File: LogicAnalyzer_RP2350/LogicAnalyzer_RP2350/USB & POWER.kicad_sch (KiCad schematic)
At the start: 14 parts, among them J2 2169890001, U1 TPS2552DRVR-1

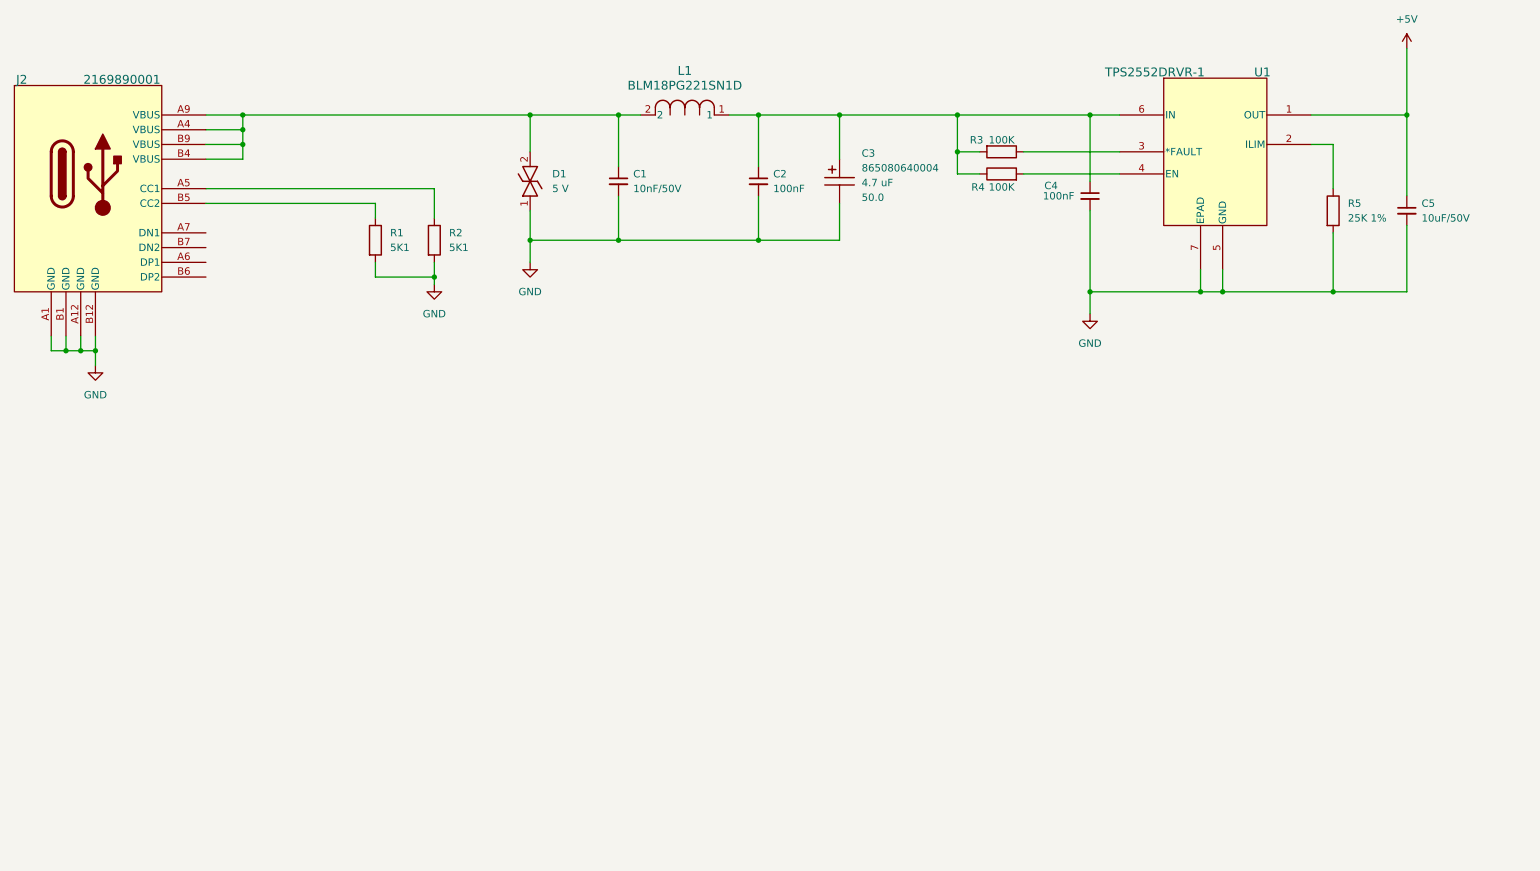
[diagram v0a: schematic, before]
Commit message: Added 3V3
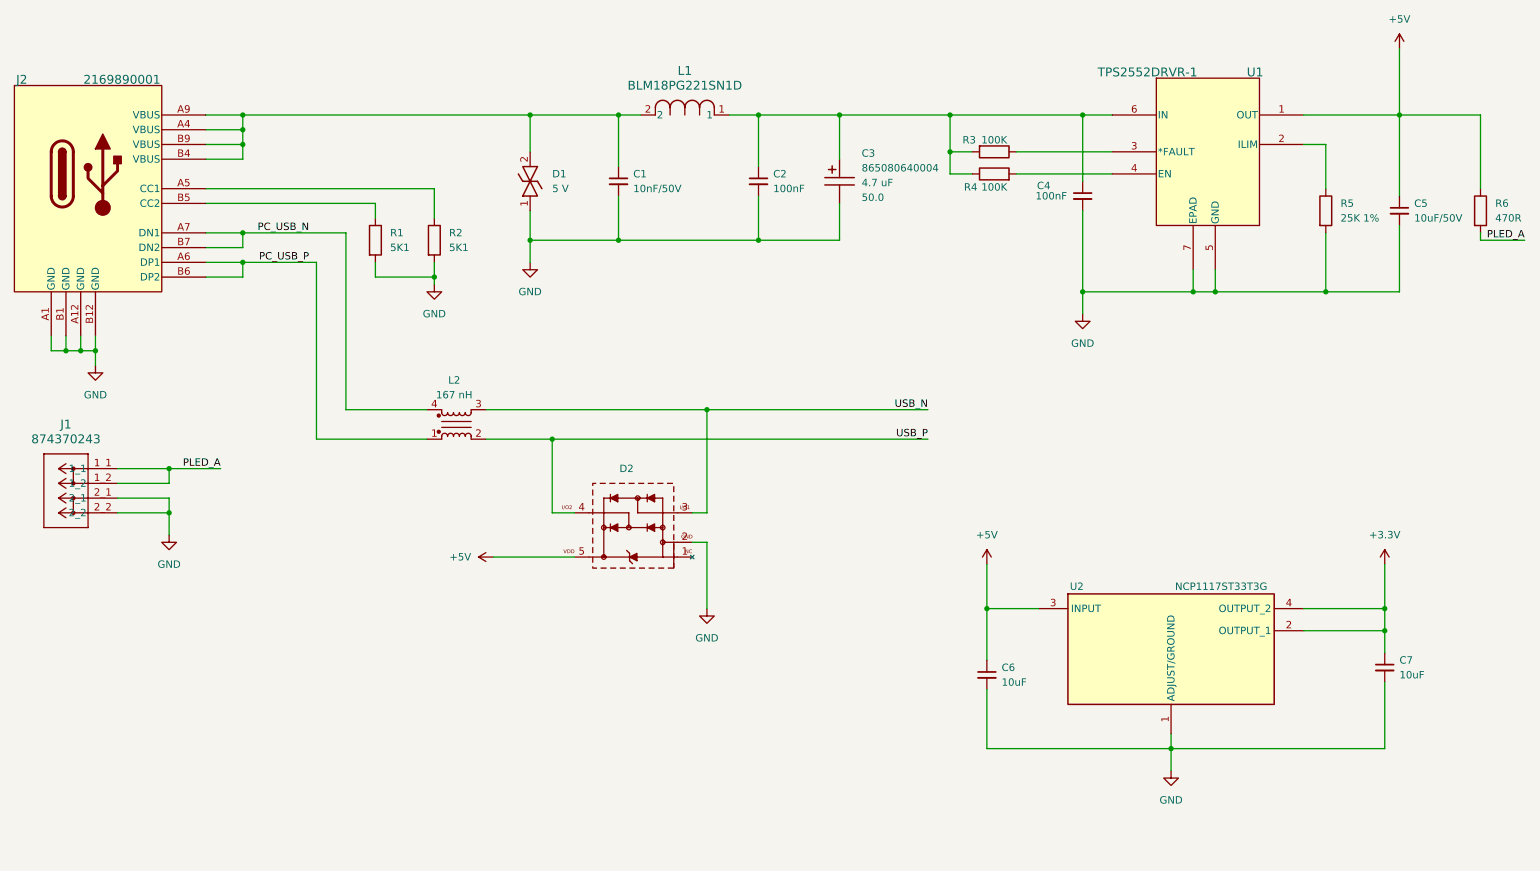
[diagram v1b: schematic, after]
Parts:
- added C6, C7: 10uF, Capacitor_SMD:C_0805_2012Metric_Pad1.18x1.45mm_HandSolder, symbol Device:C_Small
- added D2: SOT23-5L_824011, Diode_SMD_Wurth:D_Wurth_WE-TVS-SOT23-5L, symbol Diode_Wurth_WE-TVS:SOT23-5L_824011
- added J1: 874370243, CONN_874370231-SD_02_MOL, symbol Molex-0874370243:874370243
- added L2: 167 nH, Inductor_SMD_Wurth:L_Wurth_WE-CNSW-HF-0805, symbol Inductor_Wurth_WE-CNSW-HF:0805_744233121
- added R6: 470R, Resistor_SMD:R_0603_1608Metric_Pad0.98x0.95mm_HandSolder, symbol Device:R
- added U2: NCP1117ST33T3G, SOT230P700X180-4N, symbol NCP1117ST33T3G:NCP1117ST33T3G
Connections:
- net +5V: now also C6.1, D2.5 (VDD), R6.1, U2.3 (INPUT)
- net GND: now also C6.2, C7.2, D2.2 (GND), J1.2_1, J1.2_2, U2.1 (ADJUST/GROUND)
- net PC_USB_P: now reaches J2.A6 (DP1)
- net PC_USB_P: now also J2.B6 (DP2), L2.1
- net PC_USB_N: now reaches J2.A7 (DN1)
- net PC_USB_N: now also J2.B7 (DN2), L2.4
- new net +3.3V: C7.1, U2.2 (OUTPUT_1), U2.4 (OUTPUT_2)
- new net PLED_A: J1.1_1, J1.1_2, R6.2
- new net USB_N: D2.3 (I/O1), L2.3
- new net USB_P: D2.4 (I/O2), L2.2
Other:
- moved on the sheet: C4, C5, R3, R4, R5, U1

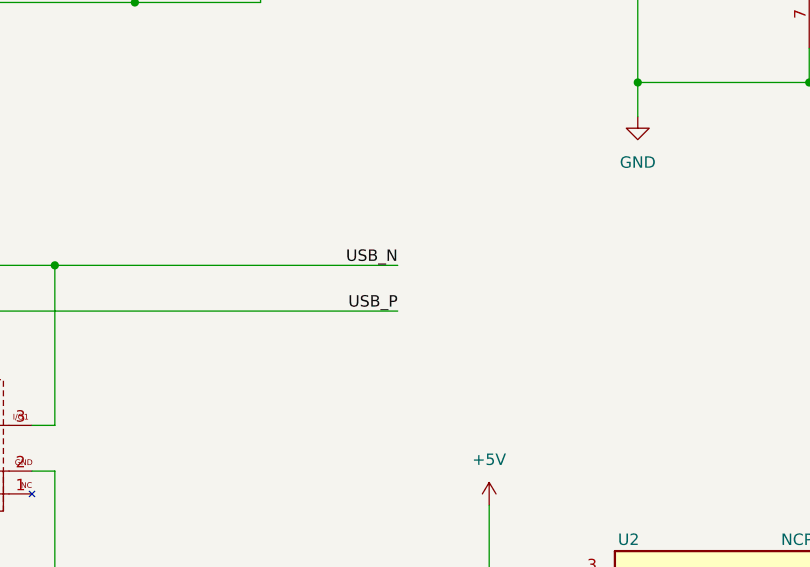
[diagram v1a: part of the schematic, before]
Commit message: added RP2350 Child Sheets and H Nets for USB
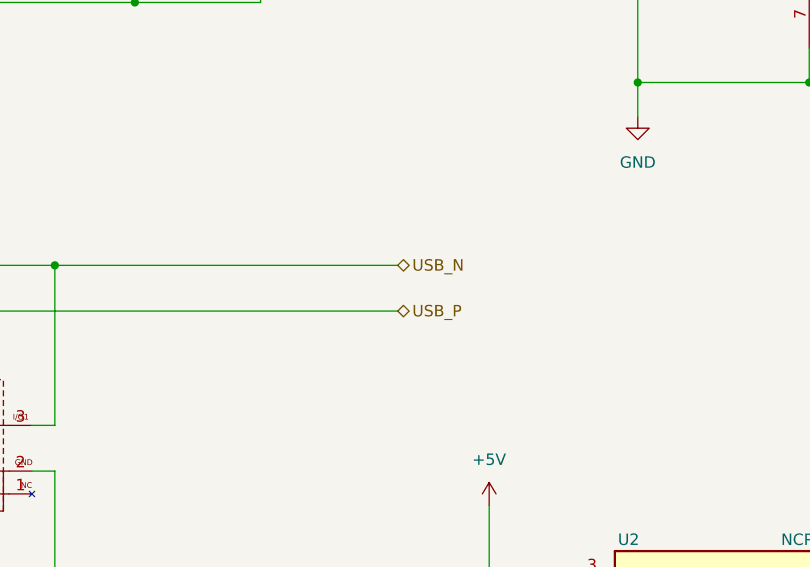
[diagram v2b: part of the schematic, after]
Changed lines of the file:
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@@
 	)
 	(junction
+		(at 114.3 90.17)
+		(diameter 0)
+		(color 0 0 0 0)
+	)
+	(junction
 		(at 257.81 123.19)
 		(diameter 0)
@@
 	)
 	(junction
-		(at 114.3 90.17)
-		(diameter 0)
-		(color 0 0 0 0)
-	)
-	(junction
 		(at 149.86 55.88)
 		(diameter 0)
@@
 		)
 	)
-	(label "USB_N"
-		(at 179.07 85.09 180)
+	(label "PC_USB_P"
+		(at 72.39 59.69 180)
 		(effects
 			(font
@@
 		)
 	)
-	(label "PC_USB_P"
-		(at 72.39 59.69 180)
+	(label "PLED_A"
+		(at 281.94 55.88 180)
 		(effects
 			(font
 				(size 1.27 1.27)
-				(color 0 0 255 1)
 			)
 			(justify right bottom)
 		)
 	)
-	(label "USB_P"
-		(at 179.07 90.17 180)
+	(label "PLED_A"
+		(at 57.15 95.25 180)
 		(effects
 			(font
 				(size 1.27 1.27)
-				(color 0 0 255 1)
 			)
 			(justify right bottom)
 		)
 	)
-	(label "PLED_A"
-		(at 281.94 55.88 180)
+	(label "PC_USB_N"
+		(at 72.39 54.61 180)
 		(effects
 			(font
 				(size 1.27 1.27)
+				(color 0 0 255 1)
 			)
 			(justify right bottom)
 		)
 	)
-	(label "PLED_A"
-		(at 57.15 95.25 180)
+	(hierarchical_label "USB_P"
+		(shape bidirectional)
+		(at 179.07 90.17 0)
 		(effects
 			(font
 				(size 1.27 1.27)
+				(color 255 153 0 1)
 			)
-			(justify right bottom)
+			(justify left)
 		)
 	)
-	(label "PC_USB_N"
-		(at 72.39 54.61 180)
+	(hierarchical_label "USB_N"
+		(shape bidirectional)
+		(at 179.07 85.09 0)
 		(effects
 			(font
 				(size 1.27 1.27)
-				(color 0 0 255 1)
+				(color 255 153 0 1)
 			)
-			(justify right bottom)
+			(justify left)
 		)
 	)
@@
 			)
 		)
-		(property "Description" "Wurth - 885012206089"
+		(property "Description" "Unpolarized capacitor, small symbol"
 			(at 125.73 45.72 0)
 			(hide yes)
@@
 			)
 		)
-		(property "Description" "Wurth 885012206095"
+		(property "Description" "Unpolarized capacitor, small symbol"
 			(at 260.35 50.8 0)
 			(hide yes)
@@
 			)
 		)
-		(property "Description" "Wurth 885012206095"
+		(property "Description" "Unpolarized capacitor, small symbol"
 			(at 205.74 48.26 0)
 			(hide yes)
@@
 			)
 		)
-		(property "Description" "Wurth 885012206095"
+		(property "Description" "Unpolarized capacitor, small symbol"
 			(at 149.86 45.72 0)
 			(hide yes)

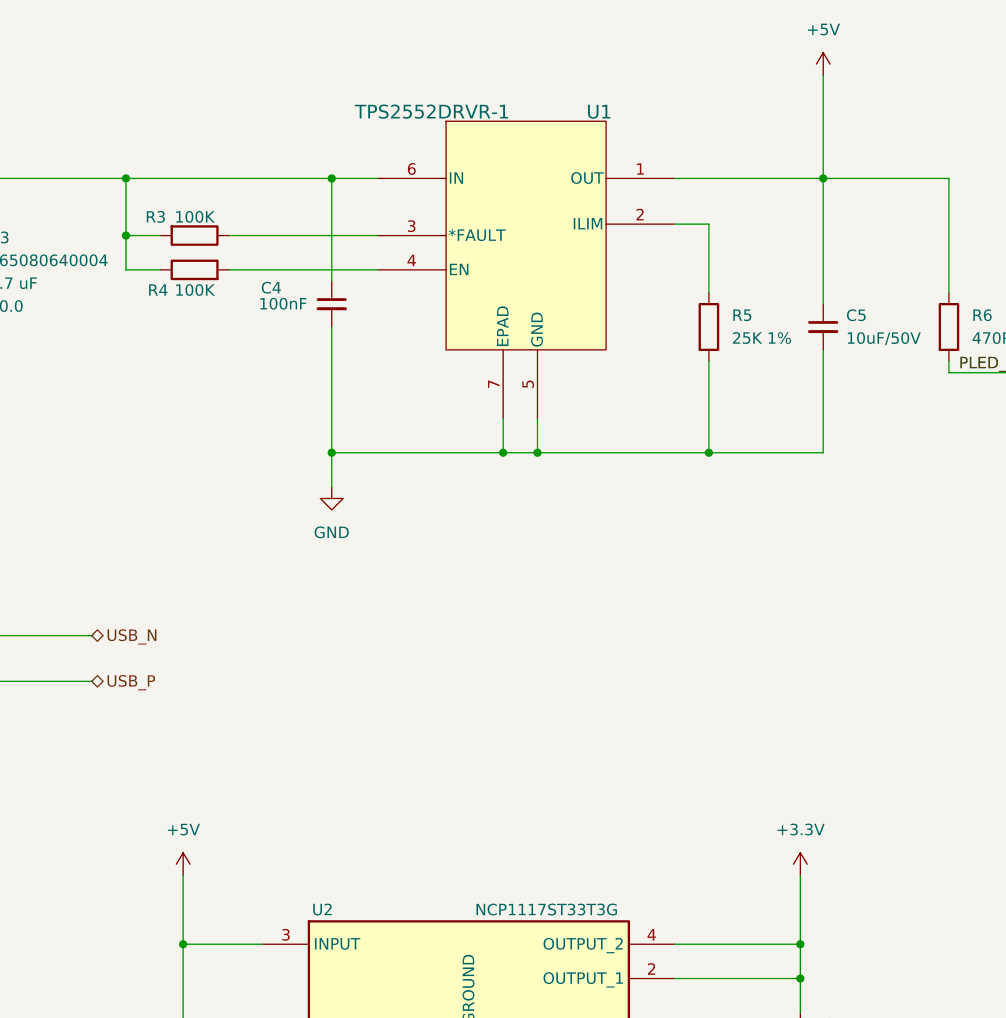
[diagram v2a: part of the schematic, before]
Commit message: Completed VREG 1V1 and Decoupling the Power Pins
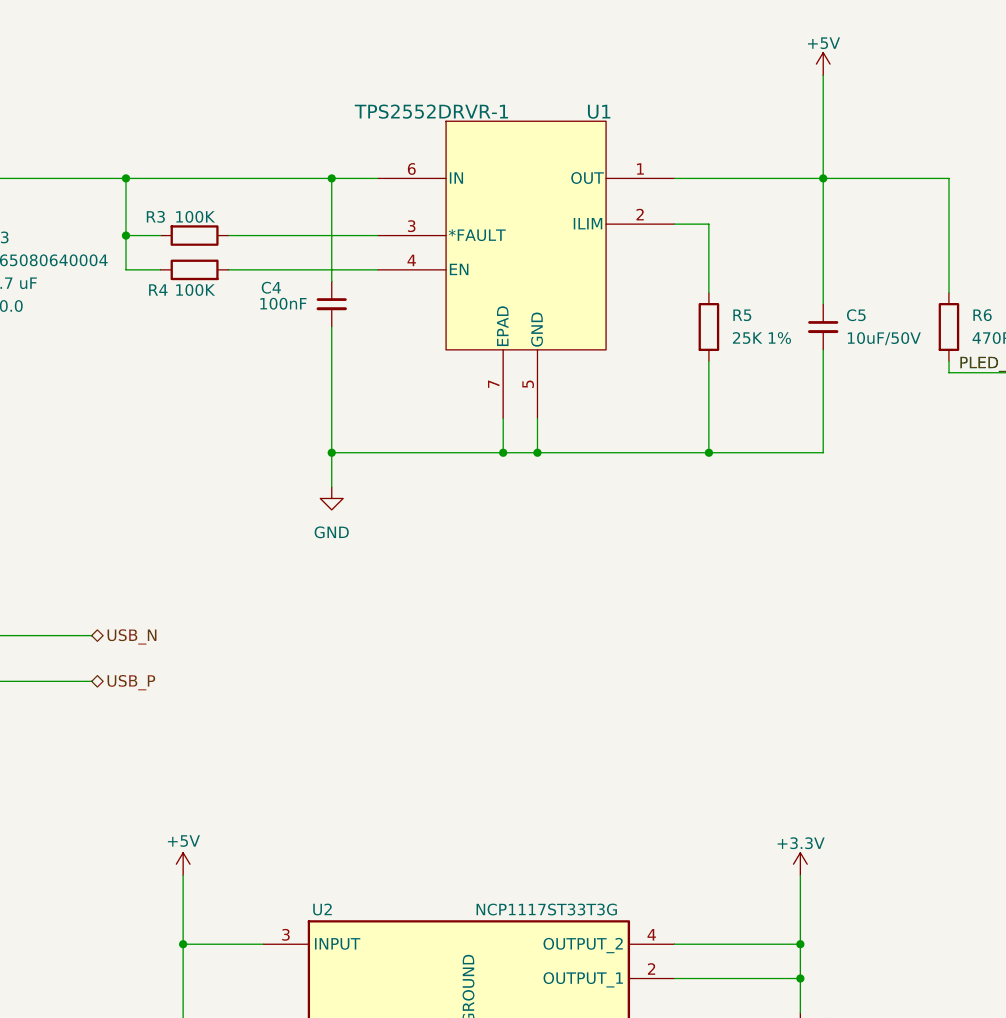
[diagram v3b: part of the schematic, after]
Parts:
- C1, C2: footprint (none) -> Capacitor_SMD:C_0805_2012Metric_Pad1.18x1.45mm_HandSolder
- C4: footprint (none) -> Capacitor_SMD:C_0603_1608Metric_Pad1.08x0.95mm_HandSolder
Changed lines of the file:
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@@
 			)
 		)
-		(property "Footprint" ""
+		(property "Footprint" "Capacitor_SMD:C_0805_2012Metric_Pad1.18x1.45mm_HandSolder"
 			(at 125.73 45.72 0)
 			(hide yes)
@@
 		(in_pos_files yes)
 		(dnp no)
-		(fields_autoplaced yes)
 		(property "Reference" "#PWR010"
 			(at 189.23 115.57 0)
@@
 		)
 		(property "Value" "+5V"
-			(at 189.23 106.68 0)
+			(at 189.23 107.95 0)
 			(show_name no)
 			(do_not_autoplace no)
@@
 		(in_pos_files yes)
 		(dnp no)
-		(fields_autoplaced yes)
 		(property "Reference" "#PWR011"
 			(at 257.81 115.57 0)
@@
 		)
 		(property "Value" "+3.3V"
-			(at 257.81 106.68 0)
+			(at 257.81 108.204 0)
 			(show_name no)
 			(do_not_autoplace no)
@@
 		(in_pos_files yes)
 		(dnp no)
-		(fields_autoplaced yes)
 		(property "Reference" "#PWR05"
 			(at 260.35 26.67 0)
@@
 		)
 		(property "Value" "+5V"
-			(at 260.35 17.78 0)
+			(at 260.35 19.304 0)
 			(show_name no)
 			(do_not_autoplace no)
@@
 			)
 		)
-		(property "Footprint" ""
+		(property "Footprint" "Capacitor_SMD:C_0603_1608Metric_Pad1.08x0.95mm_HandSolder"
 			(at 205.74 48.26 0)
 			(hide yes)
@@
 			)
 		)
-		(property "Footprint" ""
+		(property "Footprint" "Capacitor_SMD:C_0805_2012Metric_Pad1.18x1.45mm_HandSolder"
 			(at 149.86 45.72 0)
 			(hide yes)

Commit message: QSPIFLASH ADDED
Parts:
- added R14: 5K6, Resistor_SMD:R_0603_1608Metric_Pad0.98x0.95mm_HandSolder, symbol Device:R
- added R15: 10K, Resistor_SMD:R_0603_1608Metric_Pad0.98x0.95mm_HandSolder, symbol Device:R
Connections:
- net +5V: now also R14.1
- net GND: now also R15.2
- new net VBUS_SENSE: R14.2, R15.1

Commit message: Connector for Front Panel Interface Added
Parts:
- removed J1: 874370243, CONN_874370231-SD_02_MOL, symbol Molex-0874370243:874370243
- removed R6: 470R, Resistor_SMD:R_0603_1608Metric_Pad0.98x0.95mm_HandSolder, symbol Device:R

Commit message: Clearing UP ERC Errors and Warnings
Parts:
- D1: footprint Diode_SMD_Wurth:D_Wurth_WE-VE-ULC-0402 -> 82307050029-TVS-Diode_Wurth_WE-VE-ULC:D_Wurth_WE-VE-ULC-0402
- J2: footprint 216989-0001_MOL -> USBC_Molex_2169890001:216989-0001_MOL
- L1: footprint IND_BLM18_0603_MUR -> Ferrite-BLM18PG221SN1D:IND_BLM18_0603_MUR
- U1: footprint DRV6_1P6X1 -> TPS2552DRVR:DRV6_1P6X1
- U2: footprint SOT230P700X180-4N -> NCP1117:SOT230P700X180-4N
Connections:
- net at C2.1, C3.1, C4.1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: now also L1.2; no longer L1.1
- net at C1.1, D1.2, J2.A4 (VBUS)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: now also L1.1; no longer L1.2
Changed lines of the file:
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@@
 			)
 		)
-		(property "Footprint" "Diode_SMD_Wurth:D_Wurth_WE-VE-ULC-0402"
+		(property "Footprint" "82307050029-TVS-Diode_Wurth_WE-VE-ULC:D_Wurth_WE-VE-ULC-0402"
 			(at 90.17 33.02 0)
 			(hide yes)
@@
 			)
 		)
-		(property "Footprint" "216989-0001_MOL"
+		(property "Footprint" "USBC_Molex_2169890001:216989-0001_MOL"
 			(at 21.59 29.21 0)
 			(hide yes)
@@
 			)
 		)
-		(property "Footprint" "DRV6_1P6X1"
+		(property "Footprint" "TPS2552DRVR:DRV6_1P6X1"
 			(at 218.44 27.94 0)
 			(hide yes)
@@
 	)
 	(symbol
-		(lib_id "Ferrite-BLM18PG221SN1D:BLM18PG221SN1D")
-		(at 129.54 34.29 0)
-		(unit 1)
-		(body_style 1)
-		(exclude_from_sim no)
-		(in_bom yes)
-		(on_board yes)
-		(in_pos_files yes)
-		(dnp no)
-		(fields_autoplaced yes)
-		(property "Reference" "L1"
-			(at 137.16 26.67 0)
-			(show_name no)
-			(do_not_autoplace no)
-			(effects
-				(font
-					(size 1.524 1.524)
-				)
-			)
-		)
-		(property "Value" "BLM18PG221SN1D"
-			(at 137.16 29.21 0)
-			(show_name no)
-			(do_not_autoplace no)
-			(effects
-				(font
-					(size 1.524 1.524)
-				)
-			)
-		)
-		(property "Footprint" "IND_BLM18_0603_MUR"
-			(at 129.54 34.29 0)
-			(hide yes)
-			(show_name no)
-			(do_not_autoplace no)
-			(effects
-				(font
-					(size 1.27 1.27)
-					(italic yes)
-				)
-			)
-		)
-		(property "Datasheet" "BLM18PG221SN1D"
-			(at 129.54 34.29 0)
-			(hide yes)
-			(show_name no)
-			(do_not_autoplace no)
-			(effects
-				(font
-					(size 1.27 1.27)
-					(italic yes)
-				)
-			)
-		)
-		(property "Description" ""
-			(at 129.54 34.29 0)
-			(hide yes)
-			(show_name no)
-			(do_not_autoplace no)
-			(effects
-				(font
-					(size 1.27 1.27)
-				)
-			)
-		)
-		(pin "1"
-		)
-		(pin "2"
-		)
-		(instances
-			(project "LogicAnalyzer_RP2350"
-				(path "/d75f24d0-99d8-459e-8e7b-473191ec3959/805e660b-1486-4481-a006-02fc919054bd"
-					(reference "L1")
-					(unit 1)
-				)
-			)
-		)
-	)
-	(symbol
 		(lib_id "Device:R")
 		(at 247.65 50.8 0)
@@
 				(path "/d75f24d0-99d8-459e-8e7b-473191ec3959/805e660b-1486-4481-a006-02fc919054bd"
 					(reference "R5")
+					(unit 1)
+				)
+			)
+		)
+	)
+	(symbol
+		(lib_id "Ferrite-BLM18PG221SN1D:BLM18PG221SN1D")
+		(at 144.78 34.29 0)
+		(mirror y)
+		(unit 1)
+		(body_style 1)
+		(exclude_from_sim no)
+		(in_bom yes)
+		(on_board yes)
+		(in_pos_files yes)
+		(dnp no)
+		(property "Reference" "L1"
+			(at 137.16 26.67 0)
+			(show_name no)
+			(do_not_autoplace no)
+			(effects
+				(font
+					(size 1.524 1.524)
+				)
+			)
+		)
+		(property "Value" "BLM18PG221SN1D"
+			(at 137.16 29.21 0)
+			(show_name no)
+			(do_not_autoplace no)
+			(effects
+				(font
+					(size 1.524 1.524)
+				)
+			)
+		)
+		(property "Footprint" "Ferrite-BLM18PG221SN1D:IND_BLM18_0603_MUR"
+			(at 144.78 34.29 0)
+			(hide yes)
+			(show_name no)
+			(do_not_autoplace no)
+			(effects
+				(font
+					(size 1.27 1.27)
+					(italic yes)
+				)
+			)
+		)
+		(property "Datasheet" "BLM18PG221SN1D"
+			(at 144.78 34.29 0)
+			(hide yes)
+			(show_name no)
+			(do_not_autoplace no)
+			(effects
+				(font
+					(size 1.27 1.27)
+					(italic yes)
+				)
+			)
+		)
+		(property "Description" ""
+			(at 144.78 34.29 0)
+			(hide yes)
+			(show_name no)
+			(do_not_autoplace no)
+			(effects
+				(font
+					(size 1.27 1.27)
+				)
+			)
+		)
+		(pin "1"
+		)
+		(pin "2"
+		)
+		(instances
+			(project "LogicAnalyzer_RP2350"
+				(path "/d75f24d0-99d8-459e-8e7b-473191ec3959/805e660b-1486-4481-a006-02fc919054bd"
+					(reference "L1")
 					(unit 1)
 				)
@@
 			)
 		)
-		(property "Footprint" "SOT230P700X180-4N"
+		(property "Footprint" "NCP1117:SOT230P700X180-4N"
 			(at 245.11 211.76 0)
 			(hide yes)

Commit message: Net Classes Added
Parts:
- renumbered C6 to C4, C4 to C5, C7 to C6, C5 to C7, J2 to J1, L2 to L1, L1 to L2, R14 to R1, R15 to R2, R1 to R3, R2 to R4, R3 to R5, R4 to R6, R5 to R7, U2 to U1, U1 to U2
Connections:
- net VBUS_FILT: now reaches C2.1, C3.1, C5.1, L2.2, R5.2, R6.1, U2.6 (IN)
- net VBUS: now reaches C1.1, D1.2, J1.A4 (VBUS), J1.A9 (VBUS), J1.B4 (VBUS), J1.B9 (VBUS), L2.1
- net USBCC1: now reaches J1.A5 (CC1), R4.1
- net USBCC2: now reaches J1.B5 (CC2), R3.1
- net PC_USB_N renamed USBC-
- net PC_USB_P renamed USBC+
- net USB_N renamed USB-
- net USB_P renamed USB+
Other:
- note added: "3V3 LDO 1A"
- note added: "Current Limit"
- note added: "USB-C Connector"
